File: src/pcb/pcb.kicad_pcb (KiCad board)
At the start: 2 copper layers, 50 x 30 mm, 12 parts, among them J1 Conn_01x02, J2 Conn_01x02, U1 LM317_TO-220

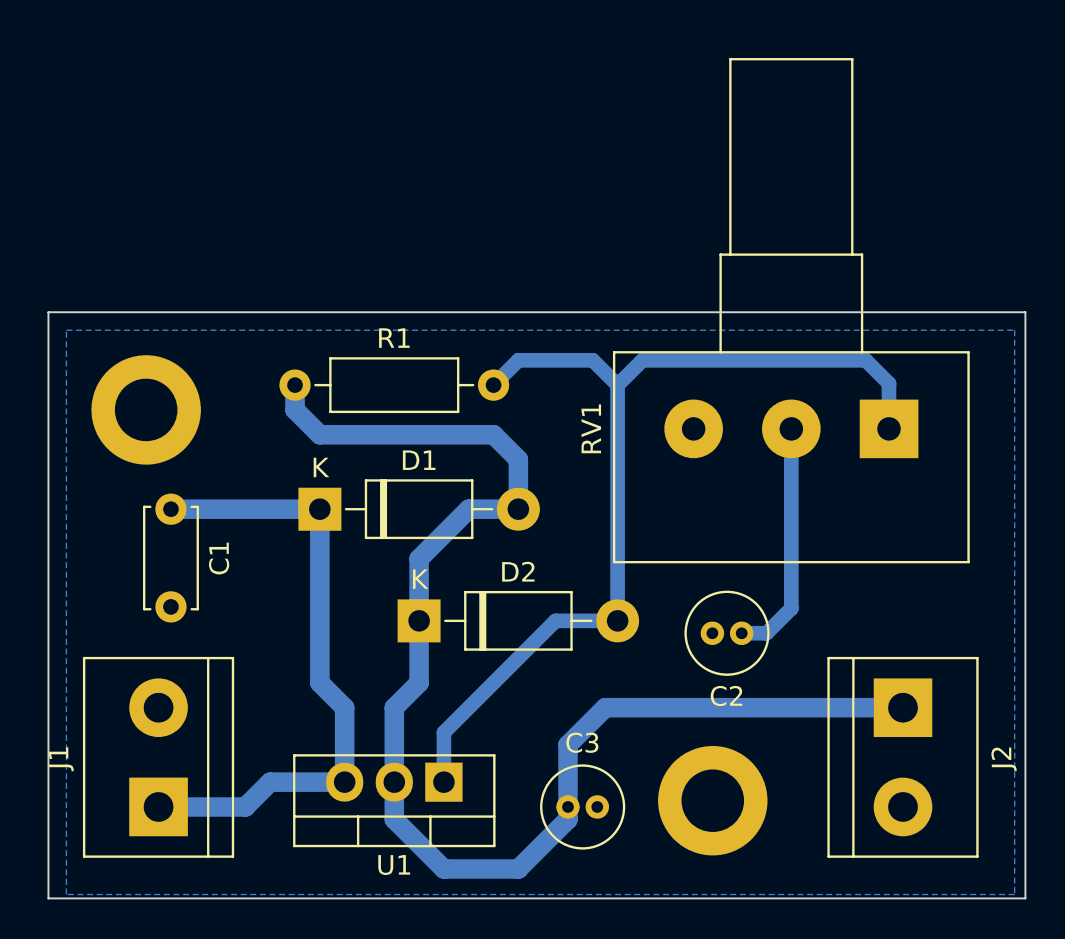
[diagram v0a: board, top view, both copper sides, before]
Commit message: Fix: Remove island
Add: Terminal Block STEP
Add: Potentiometer STEP
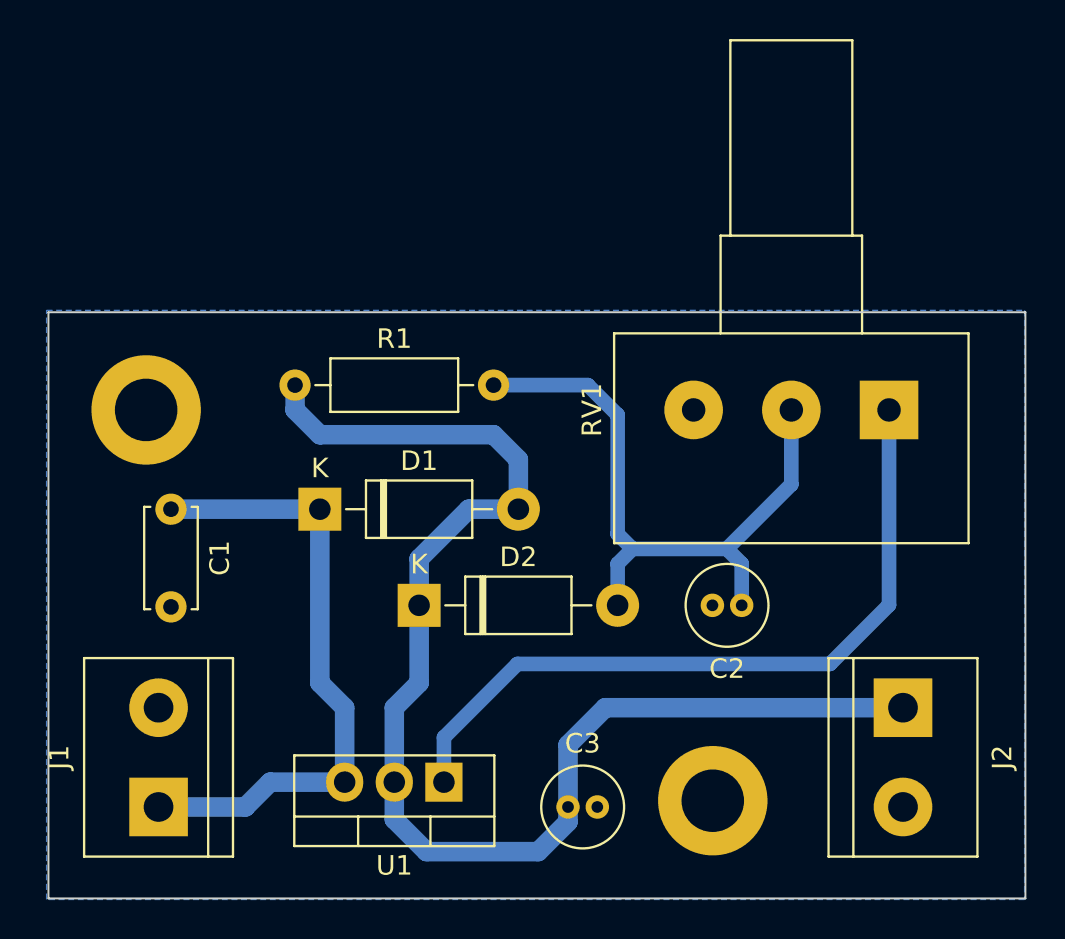
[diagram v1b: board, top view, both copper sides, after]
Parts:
- moved C2 1.43 mm to (125.7, 51.9)
- moved RV1 0.97 mm to (133.3, 41.9)
- moved D2 0.80 mm to (109.2, 51.9)
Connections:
- D2 pad 2: Net-(RV1-Pad1) -> Net-(C2-Pad1)
- R1 pad 2: Net-(RV1-Pad1) -> Net-(C2-Pad1)
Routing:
- net Net-(C2-Pad1): track 12.3 -> 33.9 mm
- net Net-(RV1-Pad1): track 50.5 -> 37.9 mm
- net Vout: track 69.0 -> 68.4 mm

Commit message: Fix: Pad Size
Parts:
- moved C3 4.19 mm to (117.9, 58.2), turned to -90 degrees
- moved C2 1.27 mm to (127.0, 51.9)
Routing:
- net Net-(C2-Pad1): track 33.9 -> 35.5 mm
- net Vout: track 68.4 -> 69.0 mm
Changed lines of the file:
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@@
     (fp_line (start 8.23 -1.25) (end 1.93 -1.25) (layer "F.Fab") (width 0.1))
     (fp_line (start 0 0) (end 1.93 0) (layer "F.Fab") (width 0.1))
-    (pad "1" thru_hole circle (at 0 0) (size 1.6 1.6) (drill 0.8) (layers *.Cu *.Mask)
+    (pad "1" thru_hole circle (at 0 0) (size 2.5 2.5) (drill 0.8) (layers *.Cu *.Mask)
       (net 5 "Vout") (pintype "passive"))
-    (pad "2" thru_hole oval (at 10.16 0) (size 1.6 1.6) (drill 0.8) (layers *.Cu *.Mask)
+    (pad "2" thru_hole circle (at 10.16 0) (size 2.5 2.5) (drill 0.8) (layers *.Cu *.Mask)
       (net 2 "Net-(C2-Pad1)") (pintype "passive"))
     (model "${KICAD6_3DMODEL_DIR}/Resistor_THT.3dshapes/R_Axial_DIN0207_L6.3mm_D2.5mm_P10.16mm_Horizontal.wrl"
@@
     (fp_line (start 5 1.25) (end 5 -1.25) (layer "F.Fab") (width 0.1))
     (fp_line (start 5 -1.25) (end 0 -1.25) (layer "F.Fab") (width 0.1))
-    (pad "1" thru_hole circle (at 0 0 270) (size 1.6 1.6) (drill 0.8) (layers *.Cu *.Mask)
+    (pad "1" thru_hole circle (at 0 0 270) (size 2.5 2.5) (drill 0.8) (layers *.Cu *.Mask)
       (net 1 "+12V") (pintype "passive"))
-    (pad "2" thru_hole circle (at 5 0 270) (size 1.6 1.6) (drill 0.8) (layers *.Cu *.Mask)
+    (pad "2" thru_hole circle (at 5 0 270) (size 2.5 2.5) (drill 0.8) (layers *.Cu *.Mask)
       (net 4 "GND") (pintype "passive"))
     (model "${KICAD6_3DMODEL_DIR}/Capacitor_THT.3dshapes/C_Disc_D5.0mm_W2.5mm_P5.00mm.wrl"
@@
     (fp_line (start 7.54 -3.15) (end -2.46 -3.15) (layer "F.Fab") (width 0.1))
     (fp_line (start -2.46 -1.88) (end 7.54 -1.88) (layer "F.Fab") (width 0.1))
-    (pad "1" thru_hole rect (at 0 0 180) (size 1.905 2) (drill 1.1) (layers *.Cu *.Mask)
+    (pad "1" thru_hole rect (at 0 0 180) (size 2 2) (drill 1.1) (layers *.Cu *.Mask)
       (net 3 "Net-(RV1-Pad1)") (pinfunction "ADJ") (pintype "input"))
-    (pad "2" thru_hole oval (at 2.54 0 180) (size 1.905 2) (drill 1.1) (layers *.Cu *.Mask)
+    (pad "2" thru_hole rect (at 2.54 0 180) (size 2 2) (drill 1.1) (layers *.Cu *.Mask)
       (net 5 "Vout") (pinfunction "VO") (pintype "power_out"))
-    (pad "3" thru_hole oval (at 5.08 0 180) (size 1.905 2) (drill 1.1) (layers *.Cu *.Mask)
+    (pad "3" thru_hole rect (at 5.08 0 180) (size 2 2) (drill 1.1) (layers *.Cu *.Mask)
       (net 1 "+12V") (pinfunction "VI") (pintype "power_in"))
     (model "${KICAD6_3DMODEL_DIR}/Package_TO_SOT_THT.3dshapes/TO-220-3_Vertical.wrl"
@@
   )
   (footprint "Capacitor_THT:C_Radial_D4.0mm_H7.0mm_P1.50mm" (layer "F.Cu")
-    (at 125.73 51.91 180)
+    (at 127 51.91 180)
     (descr "C, Radial series, Radial, pin pitch=1.50mm, diameter=4mm, height=7mm, Non-Polar Electrolytic Capacitor")
     (tags "C Radial series Radial pin pitch 1.50mm diameter 4mm height 7mm Non-Polar Electrolytic Capacitor")
@@
     (fp_circle (center 0.75 0) (end 3 0) (layer "F.CrtYd") (width 0.05) (fill none))
     (fp_circle (center 0.75 0) (end 2.75 0) (layer "F.Fab") (width 0.1) (fill none))
-    (pad "1" thru_hole circle (at 0 0 180) (size 1.2 1.2) (drill 0.6) (layers *.Cu *.Mask)
+    (pad "1" thru_hole circle (at -1.2 0 180) (size 2.5 2.5) (drill 0.8) (layers *.Cu *.Mask)
       (net 2 "Net-(C2-Pad1)") (pintype "passive"))
-    (pad "2" thru_hole circle (at 1.5 0 180) (size 1.2 1.2) (drill 0.6) (layers *.Cu *.Mask)
+    (pad "2" thru_hole circle (at 2.5 0 180) (size 2.5 2.5) (drill 0.8) (layers *.Cu *.Mask)
       (net 4 "GND") (pintype "passive"))
     (model "${KICAD6_3DMODEL_DIR}/Capacitor_THT.3dshapes/C_Radial_D4.0mm_H7.0mm_P1.50mm.wrl"
@@
   )
   (footprint "Capacitor_THT:C_Radial_D4.0mm_H7.0mm_P1.50mm" (layer "F.Cu")
-    (at 116.84 62.23)
+    (at 117.856 58.166 -90)
     (descr "C, Radial series, Radial, pin pitch=1.50mm, diameter=4mm, height=7mm, Non-Polar Electrolytic Capacitor")
     (tags "C Radial series Radial pin pitch 1.50mm diameter 4mm height 7mm Non-Polar Electrolytic Capacitor")
@@
     (property "Sheetname" "")
     (attr through_hole)
-    (fp_text reference "C3" (at 0.75 -3.25) (layer "F.SilkS")
-      (effects (font (size 1 1) (thickness 0.15)))
-    )
-    (fp_text value "1uF" (at 0.75 3.25) (layer "F.Fab")
-      (effects (font (size 1 1) (thickness 0.15)))
-    )
-    (fp_text user "${REFERENCE}" (at 0.75 0) (layer "F.Fab")
+    (fp_text reference "C3" (at 0.75 -3.25 90) (layer "F.SilkS")
+      (effects (font (size 1 1) (thickness 0.15)))
+    )
+    (fp_text value "1uF" (at 0.75 3.25 90) (layer "F.Fab")
+      (effects (font (size 1 1) (thickness 0.15)))
+    )
+    (fp_text user "${REFERENCE}" (at 0.75 0 90) (layer "F.Fab")
       (effects (font (size 0.8 0.8) (thickness 0.12)))
     )
@@
     (fp_circle (center 0.75 0) (end 3 0) (layer "F.CrtYd") (width 0.05) (fill none))
     (fp_circle (center 0.75 0) (end 2.75 0) (layer "F.Fab") (width 0.1) (fill none))
-    (pad "1" thru_hole circle (at 0 0) (size 1.2 1.2) (drill 0.6) (layers *.Cu *.Mask)
+    (pad "1" thru_hole circle (at -1.2 0 270) (size 2.5 2.5) (drill 0.8) (layers *.Cu *.Mask)
       (net 5 "Vout") (pintype "passive"))
-    (pad "2" thru_hole circle (at 1.5 0) (size 1.2 1.2) (drill 0.6) (layers *.Cu *.Mask)
+    (pad "2" thru_hole circle (at 2.7 0 270) (size 2.5 2.5) (drill 0.8) (layers *.Cu *.Mask)
       (net 4 "GND") (pintype "passive"))
     (model "${KICAD6_3DMODEL_DIR}/Capacitor_THT.3dshapes/C_Radial_D4.0mm_H7.0mm_P1.50mm.wrl"
@@
   (segment (start 96.52 46.99) (end 104.14 46.99) (width 1) (layer "B.Cu") (net 1))
   (segment (start 119.38 42.164) (end 119.38 48.26) (width 0.75) (layer "B.Cu") (net 2))
+  (segment (start 127.762 49.022) (end 128.27 48.514) (width 0.75) (layer "B.Cu") (net 2))
   (segment (start 119.38 48.26) (end 120.142 49.022) (width 0.75) (layer "B.Cu") (net 2))
-  (segment (start 128.27 45.72) (end 128.27 41.91) (width 0.75) (layer "B.Cu") (net 2))
-  (segment (start 125.73 49.784) (end 125.73 51.91) (width 0.75) (layer "B.Cu") (net 2))
-  (segment (start 120.142 49.022) (end 124.968 49.022) (width 0.75) (layer "B.Cu") (net 2))
+  (segment (start 128.6 49.86) (end 127.762 49.022) (width 0.75) (layer "B.Cu") (net 2))
+  (segment (start 128.27 48.514) (end 128.27 41.91) (width 0.75) (layer "B.Cu") (net 2))
   (segment (start 113.03 40.64) (end 117.856 40.64) (width 0.75) (layer "B.Cu") (net 2))
   (segment (start 119.38 49.784) (end 120.142 49.022) (width 0.75) (layer "B.Cu") (net 2))
-  (segment (start 124.968 49.022) (end 128.27 45.72) (width 0.75) (layer "B.Cu") (net 2))
-  (segment (start 124.968 49.022) (end 125.73 49.784) (width 0.75) (layer "B.Cu") (net 2))
+  (segment (start 127.762 49.022) (end 120.142 49.022) (width 0.75) (layer "B.Cu") (net 2))
+  (segment (start 128.6 51.91) (end 128.6 49.86) (width 0.75) (layer "B.Cu") (net 2))
   (segment (start 119.38 51.91) (end 119.38 49.784) (width 0.75) (layer "B.Cu") (net 2))
   (segment (start 117.856 40.64) (end 119.38 42.164) (width 0.75) (layer "B.Cu") (net 2))
@@
   (segment (start 133.27 51.89) (end 133.27 41.91) (width 0.75) (layer "B.Cu") (net 3))
   (segment (start 110.49 58.67) (end 114.25 54.91) (width 0.75) (layer "B.Cu") (net 3))
-  (segment (start 116.84 62.992) (end 115.316 64.516) (width 1) (layer "B.Cu") (net 5))
+  (segment (start 111.76 46.99) (end 109.22 49.53) (width 1) (layer "B.Cu") (net 5))
+  (segment (start 107.95 63.0555) (end 109.1565 64.262) (width 1) (layer "B.Cu") (net 5))
   (segment (start 113.03 43.18) (end 114.3 44.45) (width 1) (layer "B.Cu") (net 5))
   (segment (start 102.87 40.64) (end 102.87 41.91) (width 1) (layer "B.Cu") (net 5))
-  (segment (start 107.95 57.15) (end 109.22 55.88) (width 1) (layer "B.Cu") (net 5))
   (segment (start 114.3 44.45) (end 114.3 46.99) (width 1) (layer "B.Cu") (net 5))
-  (segment (start 109.601 64.516) (end 107.95 62.865) (width 1) (layer "B.Cu") (net 5))
-  (segment (start 118.745 57.15) (end 133.985 57.15) (width 1) (layer "B.Cu") (net 5))
-  (segment (start 111.76 46.99) (end 114.3 46.99) (width 1) (layer "B.Cu") (net 5))
-  (segment (start 115.316 64.516) (end 109.601 64.516) (width 1) (layer "B.Cu") (net 5))
-  (segment (start 107.95 62.865) (end 107.95 57.15) (width 1) (layer "B.Cu") (net 5))
-  (segment (start 116.84 62.23) (end 116.84 59.055) (width 1) (layer "B.Cu") (net 5))
+  (segment (start 114.3 46.99) (end 111.76 46.99) (width 1) (layer "B.Cu") (net 5))
+  (segment (start 113.284 58.42) (end 114.738 56.966) (width 1) (layer "B.Cu") (net 5))
+  (segment (start 109.22 55.88) (end 107.95 57.15) (width 1) (layer "B.Cu") (net 5))
+  (segment (start 113.284 63.246) (end 113.284 58.42) (width 1) (layer "B.Cu") (net 5))
+  (segment (start 109.22 49.53) (end 109.22 55.88) (width 1) (layer "B.Cu") (net 5))
+  (segment (start 133.813 56.978) (end 133.985 57.15) (width 1) (layer "B.Cu") (net 5))
+  (segment (start 114.738 56.966) (end 117.094 56.966) (width 1) (layer "B.Cu") (net 5))
+  (segment (start 117.048283 56.978) (end 133.813 56.978) (width 1) (layer "B.Cu") (net 5))
   (segment (start 102.87 41.91) (end 104.14 43.18) (width 1) (layer "B.Cu") (net 5))
+  (segment (start 107.95 57.15) (end 107.95 63.0555) (width 1) (layer "B.Cu") (net 5))
   (segment (start 104.14 43.18) (end 113.03 43.18) (width 1) (layer "B.Cu") (net 5))
-  (segment (start 116.84 62.23) (end 116.84 62.992) (width 1) (layer "B.Cu") (net 5))
-  (segment (start 109.22 49.53) (end 111.76 46.99) (width 1) (layer "B.Cu") (net 5))
-  (segment (start 116.84 59.055) (end 118.745 57.15) (width 1) (layer "B.Cu") (net 5))
-  (segment (start 109.22 55.88) (end 109.22 49.53) (width 1) (layer "B.Cu") (net 5))
+  (segment (start 109.1565 64.262) (end 112.268 64.262) (width 1) (layer "B.Cu") (net 5))
+  (segment (start 112.268 64.262) (end 113.284 63.246) (width 1) (layer "B.Cu") (net 5))
   (zone (net 4) (net_name "GND") (layer "B.Cu") (hatch edge 0.508)
     (connect_pads (clearance 0.508))

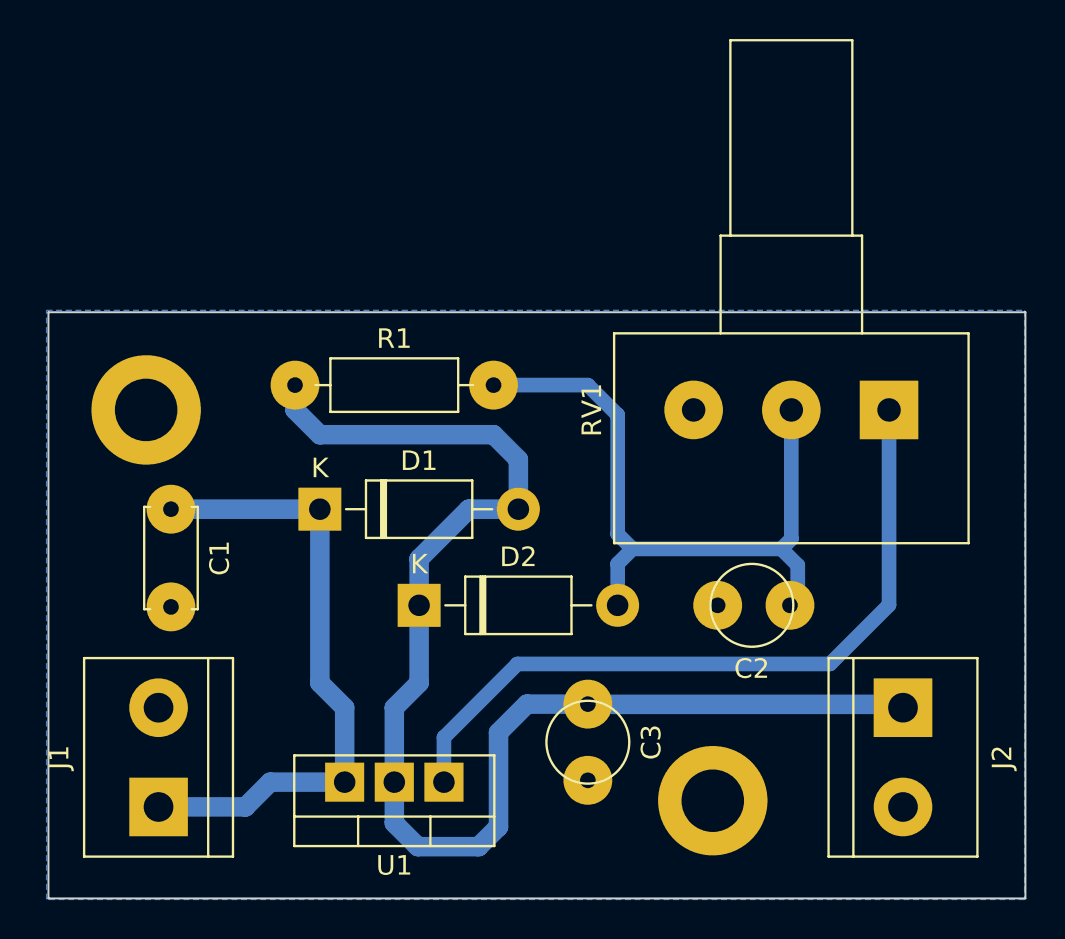
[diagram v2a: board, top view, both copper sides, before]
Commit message: Fix: Hole Sizes
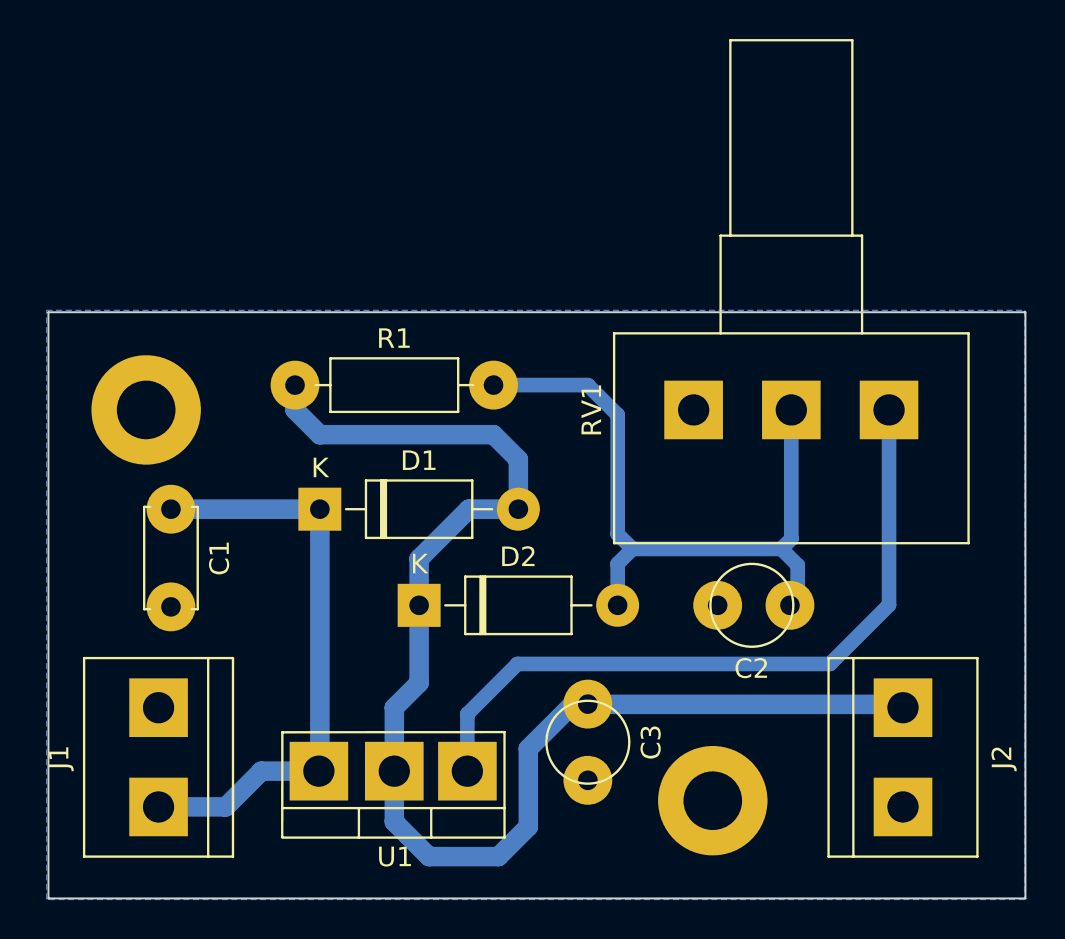
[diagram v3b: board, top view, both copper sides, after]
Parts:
- moved U1 0.76 mm to (110.5, 60.2)
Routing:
- net +12V: track 32.2 -> 30.0 mm
